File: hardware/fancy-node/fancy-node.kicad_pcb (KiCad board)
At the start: 2 copper layers, 47.1 x 30.7 mm, 63 parts, among them J1 USB_B_Micro, J2 Conn_01x06, J3 Conn_01x03, J4 Conn_01x03, J5 Conn_01x04, J6 Conn_01x02, SW1 SW_Push, SW2 SW_Push, SW3 SW_Push, SW4 SW_SPDT, U1 CH340X, U2 STM32G030C8T6, U3 WS2812b, U4 HT75xx-1-SOT89, U5 RFM69CW-915MHZ, U6 TP4056

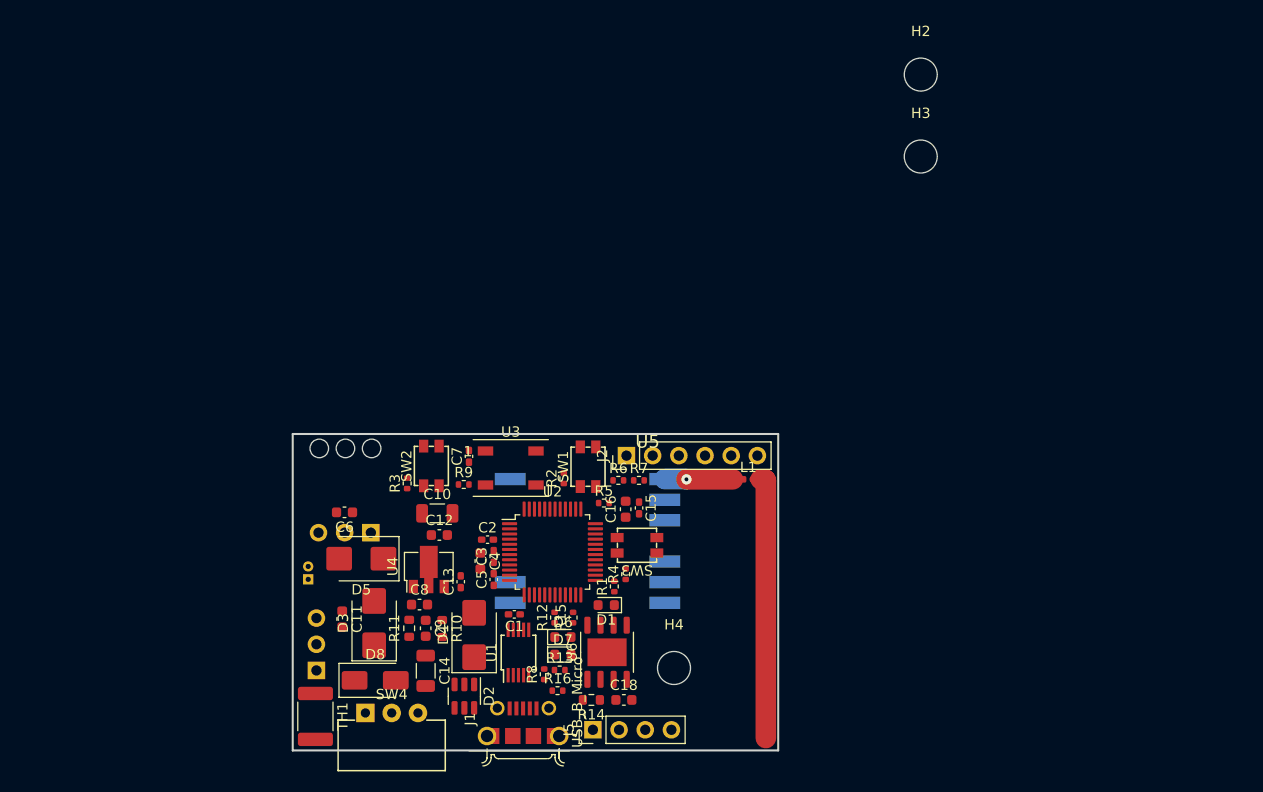
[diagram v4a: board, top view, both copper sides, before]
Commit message: Complete routing for fancy-node v1.2
Change-Id: I592d8a70fb0dd3ce7e678b66b73a8dfb2f1c9b60
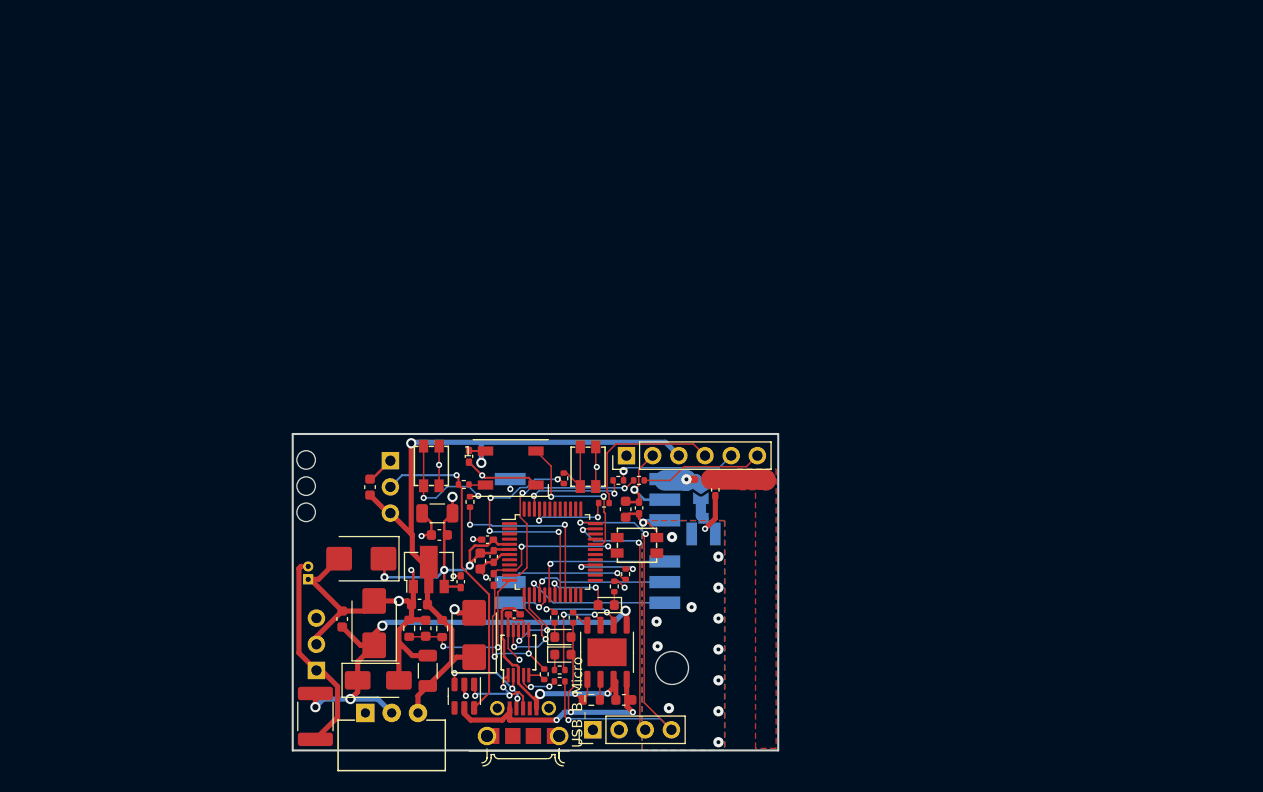
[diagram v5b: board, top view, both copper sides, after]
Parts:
- removed H2, H3: MountingHole, MountingHole:MountingHole_3.2mm_M3
- added C17: 1pF, Capacitor_SMD:C_0402_1005Metric_Pad0.74x0.62mm_HandSolder, F.Cu at (93.7, 91.2)
- added J7: 2337019-1, Homebrew:CONN_2337019-1, B.Cu at (92.6, 95.5)
- added JP2: SolderJumper_2_Open, Jumper:SolderJumper-2_P1.3mm_Open_TrianglePad1.0x1.5mm, B.Cu at (92.3, 91.4)
- moved J3 7.23 mm to (62.2, 88.4), turned to 180 degrees
- moved R3 6.36 mm to (69.9, 92.4)
- moved H1 5.29 mm to (54.0, 90.9), turned to 90 degrees
- moved L1 4.72 mm to (92.2, 90.2)
- moved C6 3.48 mm to (60.2, 91.0), turned to -90 degrees
- moved R16 0.92 mm to (78.6, 109.8)
- moved D8 0.30 mm to (61.0, 109.7)
- moved C14 0.20 mm to (65.8, 108.8)
- moved H4 0.19 mm to (89.5, 108.5)
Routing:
- net GND: track 0.00 -> 107.0 mm, vias 0 -> 30
- net +BATT: track 0.00 -> 66.6 mm, vias 0 -> 2
- net VCC: track 0.00 -> 48.8 mm, vias 0 -> 6
- net /BATT_DIRECT: track 0.00 -> 47.5 mm, vias 0 -> 4
- net /BOOT0: track 0.00 -> 42.9 mm, vias 0 -> 3
- net VBUS: track 0.00 -> 31.7 mm, vias 0 -> 3
- net /EXTERNAL_LED: track 0.00 -> 31.4 mm, vias 0 -> 1
- net /SWDIO: track 0.00 -> 24.9 mm, vias 0 -> 2
- net Net-(U2-PB1): track 0.00 -> 24.2 mm, vias 0 -> 4
- net /AUX2: track 0.00 -> 20.9 mm, vias 0 -> 2
- net /ANTENNA: track 26.3 -> 5.34 mm
- net Net-(J4-Pin_1): track 0.00 -> 19.8 mm
- net Net-(U2-PB2): track 0.00 -> 17.8 mm, vias 0 -> 2
- net /VBATT_DIV: track 0.00 -> 16.5 mm, vias 0 -> 2
- net Net-(J2-Pin_4): track 0.00 -> 15.3 mm
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- added copper zone on F.Cu, net /ANTENNA
- added copper zone on B.Cu, net GND
- added copper zone on F.Cu, net GND
- added copper zone on In1.Cu, net GND
- added copper zone on In2.Cu, net GND
- added copper zone on In2.Cu, net VCC
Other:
- copper layers 2 -> 4

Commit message: Generate fab files for fancy-node v1.2
Change-Id: If2130e4a93829307ed5471cd4c6d67e4a752f069
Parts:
- C9: value 10uF -> 100nF; footprint Capacitor_SMD:C_0603_1608Metric -> Capacitor_SMD:C_0402_1005Metric_Pad0.74x0.62mm_HandSolder
- U3: footprint LED_SMD:LED_WS2812B_PLCC4_5.0x5.0mm_P3.2mm -> Homebrew:LED_XINGLIGHT_WS2812B_PLCC4_5.0x5.0mm_P3.2mm
- moved C9 0.22 mm to (65.4, 104.7), turned to 90 degrees
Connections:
- net Net-(JP2-B) renamed /ANTENNA_UFL
- C9 pad 1: GND -> /VBATT_DIV
- C9 pad 2: /VBATT_DIV -> GND
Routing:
- net VCC: track 48.8 -> 46.7 mm
- net Net-(U1-~{RTS}): track 4.16 -> 4.85 mm, vias 2 -> 0
- net /ANTENNA: track 5.34 -> 4.80 mm
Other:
- board text added: "+"
- board text added: "+BATT"
- board text added: "-"
- board text added: "0"
- board text added: "1"
- board text added: "2"
- board text added: "3"
- board text added: "3V3"
- board text added: "A0"
- board text added: "A1"
- board text added: "A2"
- board text added: "B"
- board text added: "CLK"
- board text added: "G"
- board text added: "GND"
- board text added: "IO"
- board text added: "LED"
- board text added: "OFF"
- board text added: "ON"
- board text added: "RESET"
- board text added: "fancy-node v1.2"

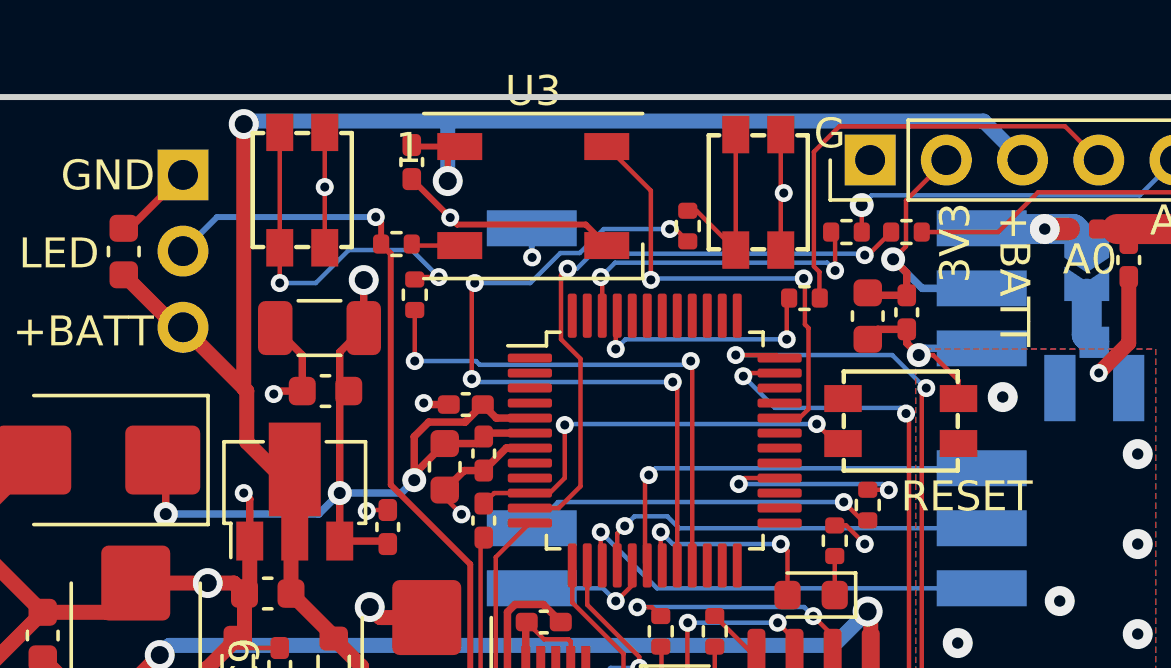
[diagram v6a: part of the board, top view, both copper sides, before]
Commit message: DFM tweaks for fancy-node v1.2
Change-Id: I792b47978d6c444ab90a5a071e11440810b06c61
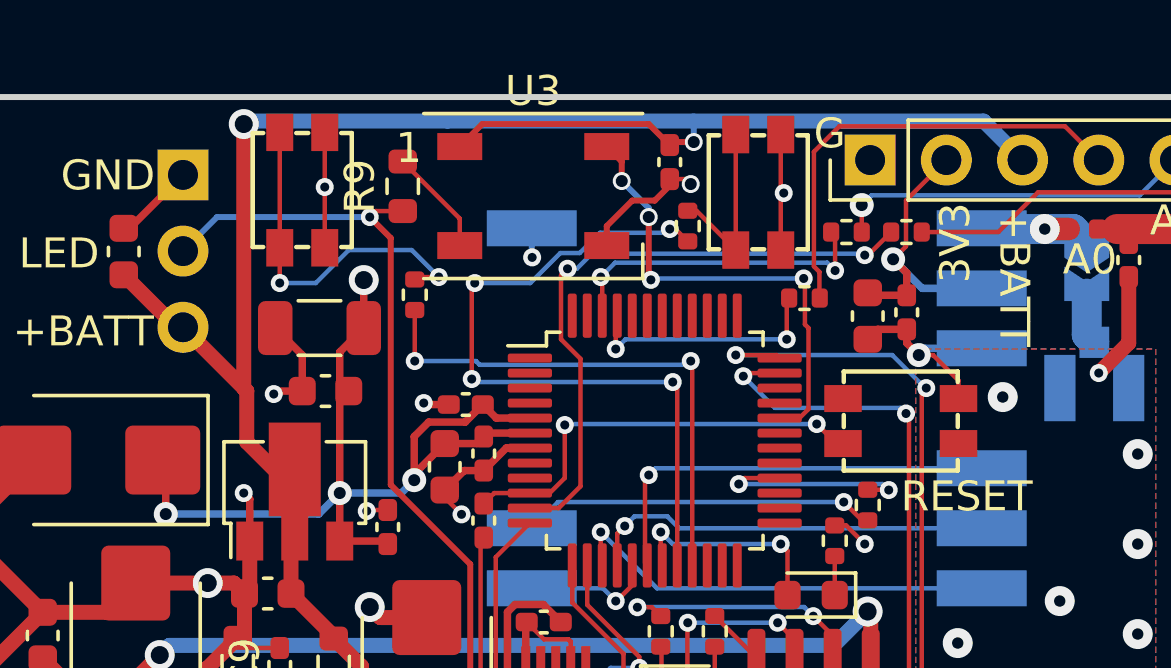
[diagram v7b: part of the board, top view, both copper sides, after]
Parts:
- R9: value 33 -> 470; footprint Resistor_SMD:R_0402_1005Metric -> Resistor_SMD:R_0603_1608Metric
- moved C7 8.60 mm to (78.4, 88.0)
- moved R9 1.94 mm to (69.5, 88.8), turned to 90 degrees
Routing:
- net +BATT: track 66.6 -> 70.9 mm
- net GND: track 106.9 -> 103.8 mm
- net Net-(U3-DOUT): track 1.55 -> 3.59 mm
- net /EXTERNAL_LED: track 31.4 -> 32.4 mm
- net /INTERNAL_LED: vias 2 -> 4

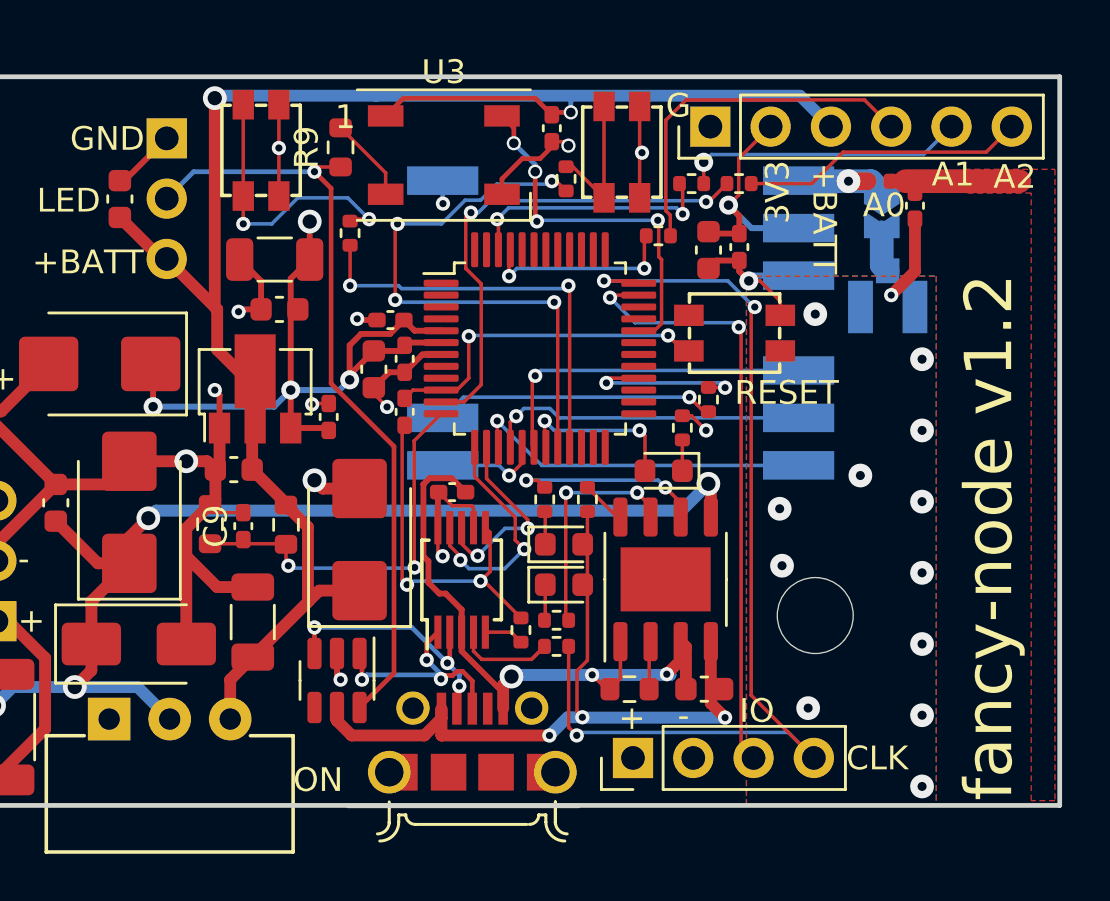
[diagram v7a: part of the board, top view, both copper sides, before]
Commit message: fancy-node v1.3:
- Migrate to MCU with 128kB of flash, from 64kB
- Fix power switch labels
- Fix bootloader: use "One-click USB download of MCU" configuration from CH340 datasheet
- Update pi filter for antenna tuning, based on NanoVNA measurement

Change-Id: I47198b318729be310c11fabc2dad25f322eb5a4f
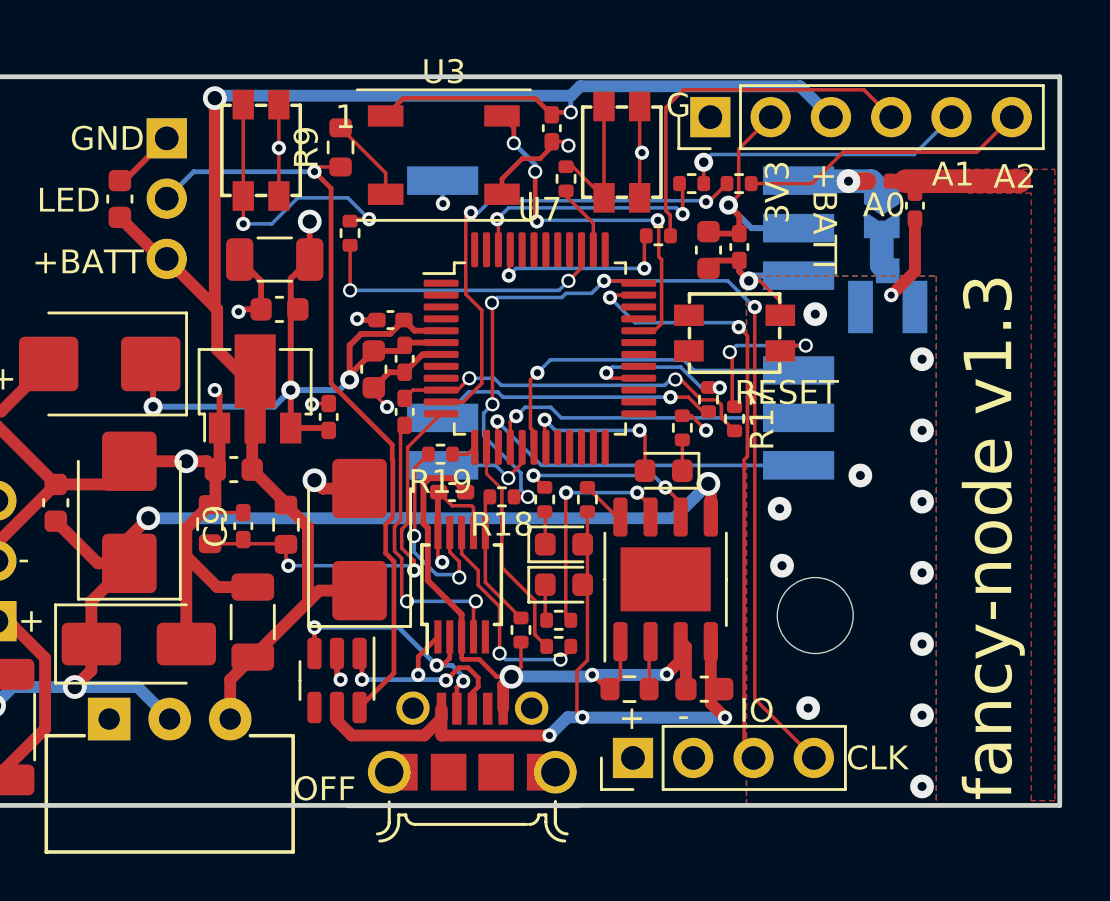
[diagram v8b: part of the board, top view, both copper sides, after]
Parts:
- removed U2: STM32G030C8T6, Package_QFP:LQFP-48_7x7mm_P0.5mm
- added R17: 1k, Resistor_SMD:R_0402_1005Metric, F.Cu at (86.1, 100.2)
- added R18: 10k, Resistor_SMD:R_0402_1005Metric, F.Cu at (76.3, 103.5)
- added R19: 220, Resistor_SMD:R_0402_1005Metric, F.Cu at (73.7, 101.7)
- added U7: STM32G070CBTx, Package_QFP:LQFP-48_7x7mm_P0.5mm, F.Cu at (77.9, 97.2)
- R16: value 4k7 -> 220
- moved J2 0.40 mm to (85.1, 87.5)
- moved U1 0.20 mm to (74.6, 107.2)
- moved R13 0.09 mm to (78.7, 108.7)
- moved R16 0.09 mm to (78.7, 109.8)
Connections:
- C5 pad 1: /~{DTR} -> /~{RTS}
- C5 pad 2: Net-(U2-NRST) -> Net-(U7-NRST)
- D1 pad 2: Net-(D1-A) -> /LED
- R16 pad 1: Net-(U1-~{RTS}) -> /USART_RX
- R16 pad 2: /BOOT0 -> Net-(U1-TXD)
- R2 pad 1: Net-(U2-PB1) -> /SW1
- R3 pad 1: Net-(U2-PB2) -> /SW2
- R8 pad 1: Net-(U1-~{CTS}) -> GND
- R8 pad 2: /~{DTR} -> Net-(U1-TNOW/~{DTR})
- SW3 pad 1: Net-(U2-NRST) -> Net-(R17-Pad1)
- U1 pad 4: Net-(U1-~{RTS}) -> /~{RTS}
- U1 pad 5: Net-(U1-~{CTS}) -> unconnected-(U1-~{CTS}-Pad5)
- U1 pad 6: /~{DTR} -> Net-(U1-TNOW/~{DTR})
- U1 pad 8: /USART_RX -> Net-(U1-TXD)
- U1 pad 9: /USART_TX -> Net-(U1-RXD)
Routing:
- net Net-(U2-PB1): track 24.2 -> 0.00 mm, vias 4 -> 0
- net Net-(U2-PB2): track 17.8 -> 0.00 mm, vias 2 -> 0
- net Net-(U7-NRST): track 0.00 -> 15.7 mm, vias 0 -> 2
- net /~{DTR}: track 14.8 -> 0.00 mm, vias 2 -> 0
- net Net-(U2-NRST): track 13.5 -> 0.00 mm, vias 2 -> 0
- net /SW2: track 0.00 -> 12.8 mm, vias 0 -> 2
- net /~{RTS}: track 0.00 -> 12.0 mm, vias 0 -> 2
- net Net-(U1-TXD): track 0.00 -> 9.05 mm, vias 0 -> 2
- net /USART_TX: track 9.88 -> 1.05 mm, vias 2 -> 0
- net Net-(U1-RXD): track 0.00 -> 8.79 mm, vias 0 -> 2
- net /LED: track 0.00 -> 7.09 mm, vias 0 -> 2
- net Net-(D1-A): track 7.02 -> 0.00 mm, vias 2 -> 0
- net Net-(R17-Pad1): track 0.00 -> 6.51 mm, vias 0 -> 2
- net Net-(U1-TNOW/~{DTR}): track 0.00 -> 5.53 mm
- net Net-(U1-~{RTS}): track 4.85 -> 0.00 mm
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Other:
- board text added: "fancy-node v1.3"
- board text removed: "fancy-node v1.2"
